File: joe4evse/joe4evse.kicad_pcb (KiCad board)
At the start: 2 copper layers, 100 x 100 mm, 85 parts, among them J1 USB_B_Micro, J10 Conn_01x02, J11 Conn_01x02, J12 Conn_02x06_Odd_Even, J13 Conn_01x03, J14 Conn_01x02, J2 Conn_01x03, J3 Conn_01x03, J4 Conn_01x02, J5 Conn_01x03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

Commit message: joe/pcb: Rev 1.1
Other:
- board text added: "Dalton EVSE "Joe" Board rev. 1.1 (c) Tuetuopay 2019-2020"
- board text removed: "Dalton EVSE "Joe" Board rev. 1.0 (c) Tuetuopay 2019"
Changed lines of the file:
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@@
     (effects (font (size 1 1) (thickness 0.15)))
   )
-  (gr_text "Dalton EVSE\n\"Joe\" Board rev. 1.0\n(c) Tuetuopay 2019" (at 182 132.4) (layer F.SilkS)
+  (gr_text "Dalton EVSE\n\"Joe\" Board rev. 1.1\n(c) Tuetuopay 2019-2020" (at 180.9 132.4) (layer F.SilkS)
     (effects (font (size 1 1) (thickness 0.15)) (justify left))
   )

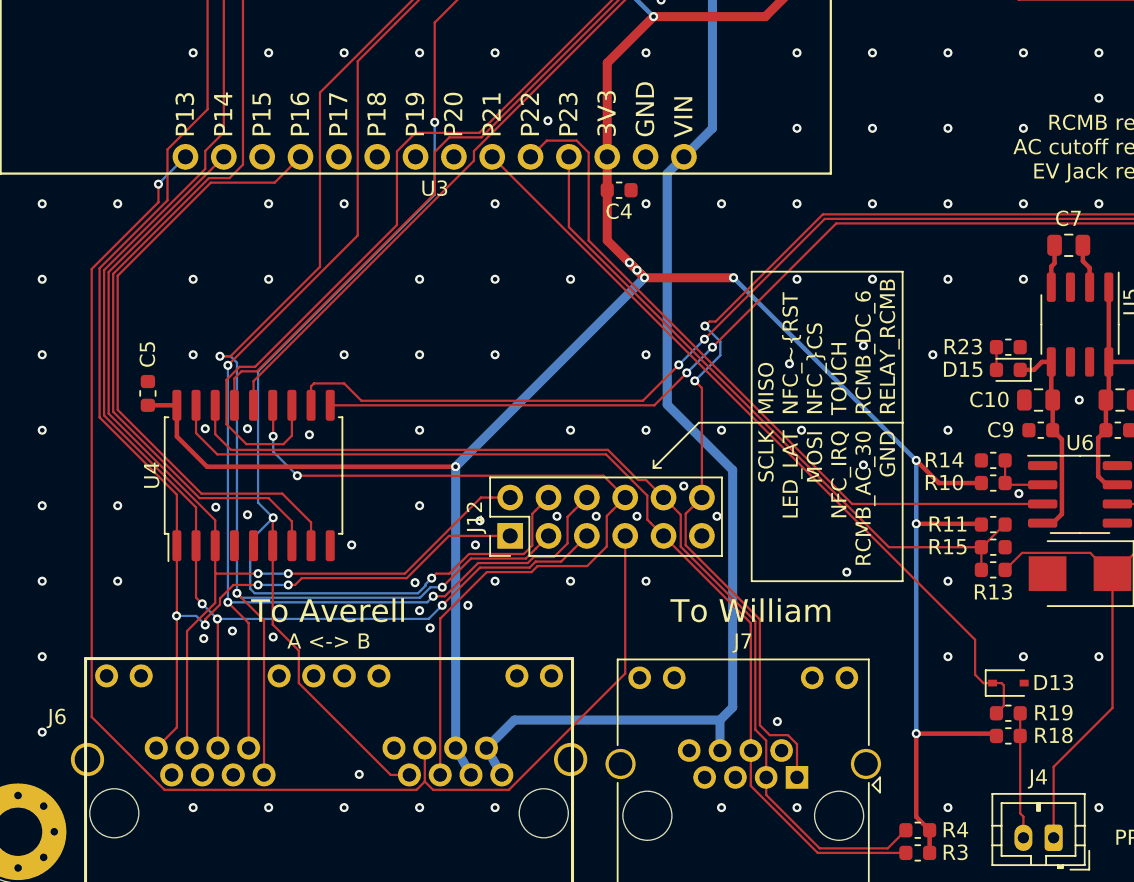
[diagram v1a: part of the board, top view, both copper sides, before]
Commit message: joe/{sch, pcb}: Swap some MCU pins for easier pinout
- Swap P23/P13
- Swap P21/P16
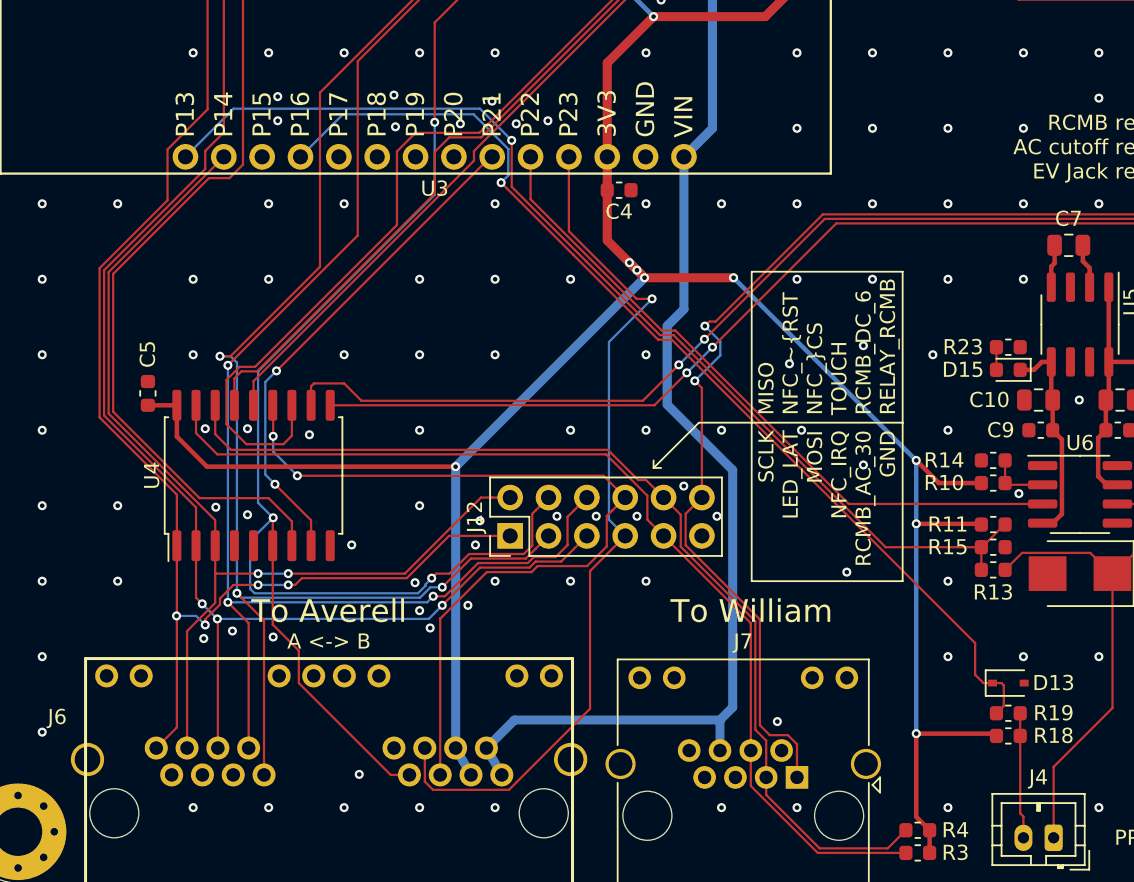
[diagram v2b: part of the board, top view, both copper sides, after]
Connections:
- U3 pad 15: /NFC_IRQ -> /fipy/PILOT_IN
- U3 pad 18: /fipy/IO_IRQ -> /fipy/PP_IN
- U3 pad 23: /fipy/PP_IN -> /fipy/IO_IRQ
- U3 pad 25: /fipy/PILOT_IN -> /NFC_IRQ
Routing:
- net /NFC_IRQ: track 92.0 -> 57.7 mm
- net /fipy/PILOT_IN: track 44.5 -> 71.6 mm, vias 0 -> 1
- net /fipy/PP_IN: track 51.8 -> 68.7 mm, vias 0 -> 1
- net /fipy/IO_IRQ: track 41.7 -> 33.3 mm, vias 0 -> 2
- net /evse/PILOT_IN: track 47.8 -> 45.1 mm
- net GND: vias 213 -> 220

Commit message: joe/pcb: Fix D13 footprint
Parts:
- D13: footprint Diode_SMD:D_SOD-323 -> Diode_SMD:D_SOD-123
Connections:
- U4 pad 8: /fipy/IO_IRQ -> Net-(U4-Pad8)

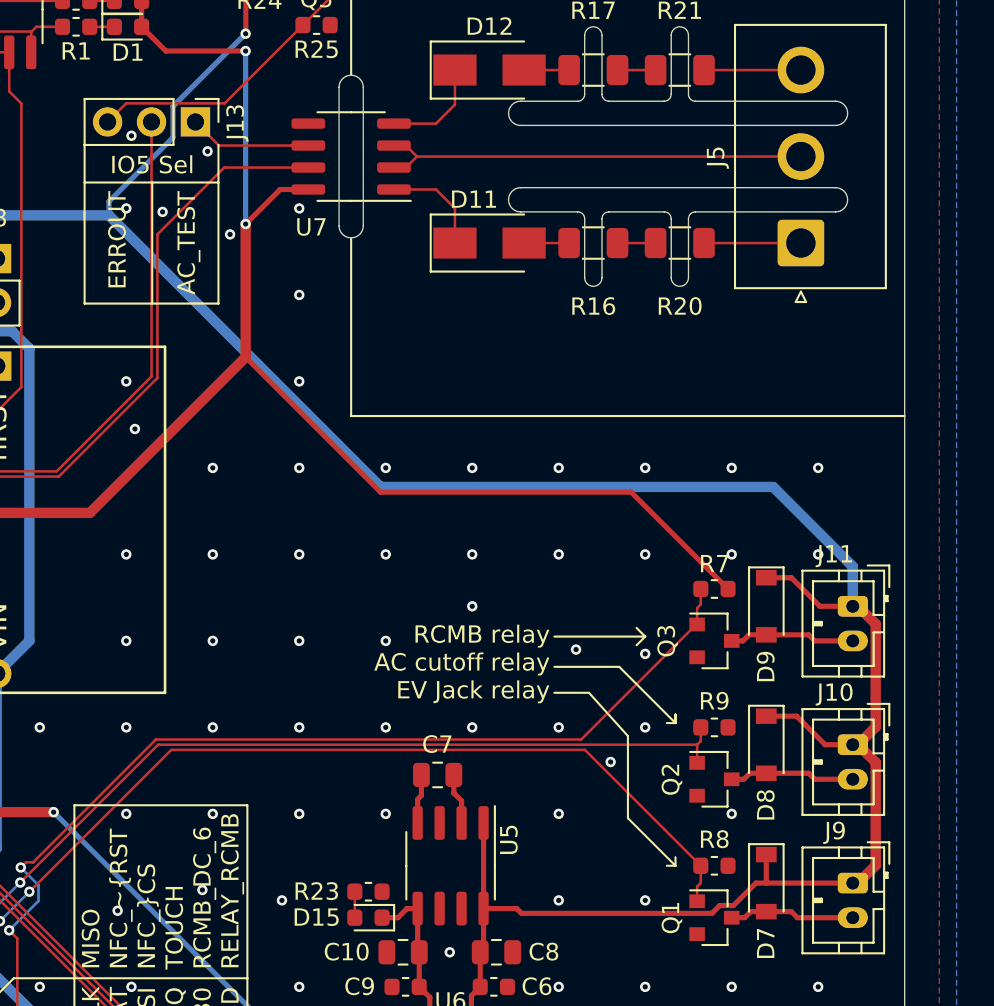
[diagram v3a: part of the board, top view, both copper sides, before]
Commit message: joe/{sch, pcb}: Combine AC_RELAY and RCMB output
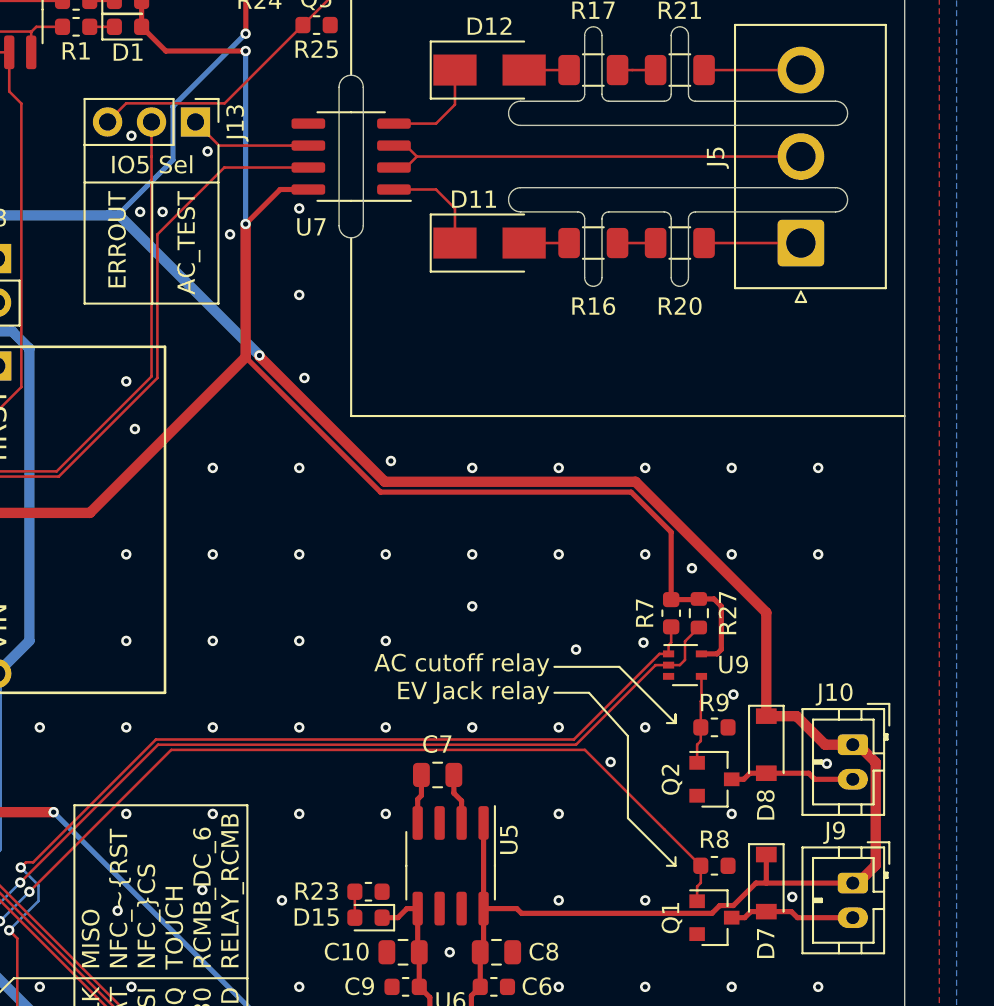
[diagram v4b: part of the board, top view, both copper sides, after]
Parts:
- removed D9: D_Schottky, Diode_SMD:D_SOD-123
- removed J11: Conn_01x02, Connector_JST:JST_PH_B2B-PH-K_1x02_P2.00mm_Vertical
- removed Q3: AO3402, Package_TO_SOT_SMD:SOT-23
- added R27: 10k, Resistor_SMD:R_0603_1608Metric, F.Cu at (188.1, 98.4)
- added U9: 74LVC1G02, Package_TO_SOT_SMD:SOT-353_SC-70-5, F.Cu at (187.3, 101.4)
- moved R7 2.87 mm to (186.5, 98.4), turned to 270 degrees
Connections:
- Q2 pad 1: /RELAY_AC -> Net-(Q2-Pad1)
- R7 pad 1: /RELAY_RCMB -> +3V3
- R7 pad 2: +3V3 -> /RELAY_RCMB
- R9 pad 2: /RELAY_AC -> Net-(Q2-Pad1)
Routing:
- net +12V: track 203.3 -> 188.5 mm, vias 4 -> 5
- net Net-(D9-Pad2): track 7.29 -> 0.00 mm
- net +3V3: track 298.5 -> 304.6 mm
- net Net-(Q2-Pad1): track 0.00 -> 5.10 mm
- net /RELAY_RCMB: track 82.5 -> 79.6 mm
- net /RELAY_AC: track 74.1 -> 75.5 mm
- net GND: vias 220 -> 224
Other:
- board text added: "AC cutoff relay EV Jack relay"
- board text removed: "RCMB relay AC cutoff relay EV Jack relay"

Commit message: joe/{sch, pcb}: Remove input shottky diodes
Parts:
- removed D3, D4: D_Schottky, Diode_SMD:D_SOD-123
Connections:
- J3 pad 2: Net-(D4-Pad2) -> +5V
- J3 pad 3: Net-(D3-Pad2) -> +12V
- U4 pad 8: Net-(U4-Pad8) -> /fipy/IO_IRQ
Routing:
- net +12V: track 188.5 -> 202.0 mm
- net +5V: track 168.3 -> 175.6 mm
- net Net-(D4-Pad2): track 4.00 -> 0.00 mm
- net Net-(D3-Pad2): track 4.00 -> 0.00 mm

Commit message: joe/pcb: Rev 1.2
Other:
- board text added: "Dalton EVSE "Joe" Board rev. 1.2 (c) Tuetuopay 2019-2021"
- board text removed: "Dalton EVSE "Joe" Board rev. 1.1 (c) Tuetuopay 2019-2020"
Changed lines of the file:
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@@
     (effects (font (size 1 1) (thickness 0.15)))
   )
-  (gr_text "Dalton EVSE\n\"Joe\" Board rev. 1.1\n(c) Tuetuopay 2019-2020" (at 180.9 132.4) (layer F.SilkS)
+  (gr_text "Dalton EVSE\n\"Joe\" Board rev. 1.2\n(c) Tuetuopay 2019-2021" (at 180.9 132.4) (layer F.SilkS)
     (effects (font (size 1 1) (thickness 0.15)) (justify left))
   )

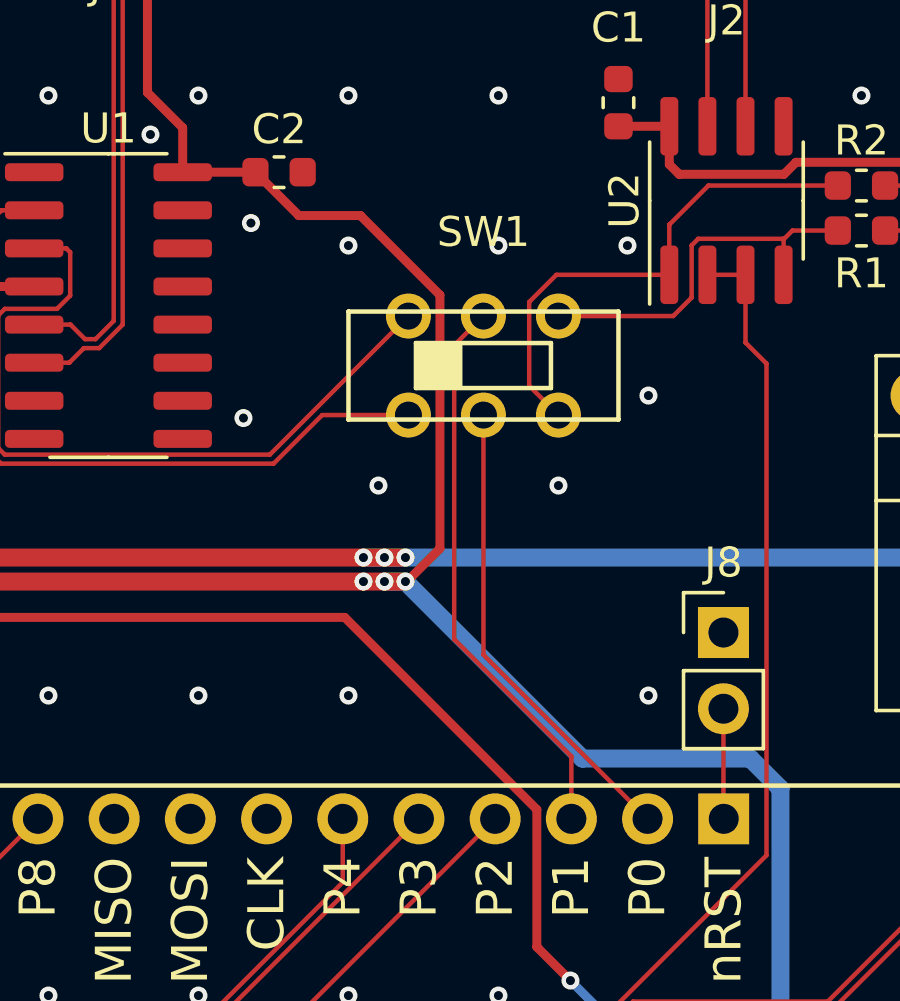
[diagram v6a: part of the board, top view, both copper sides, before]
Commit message: joe/{sch, pcb}: Add 0r resistors in parallel of SW1 for prod boards
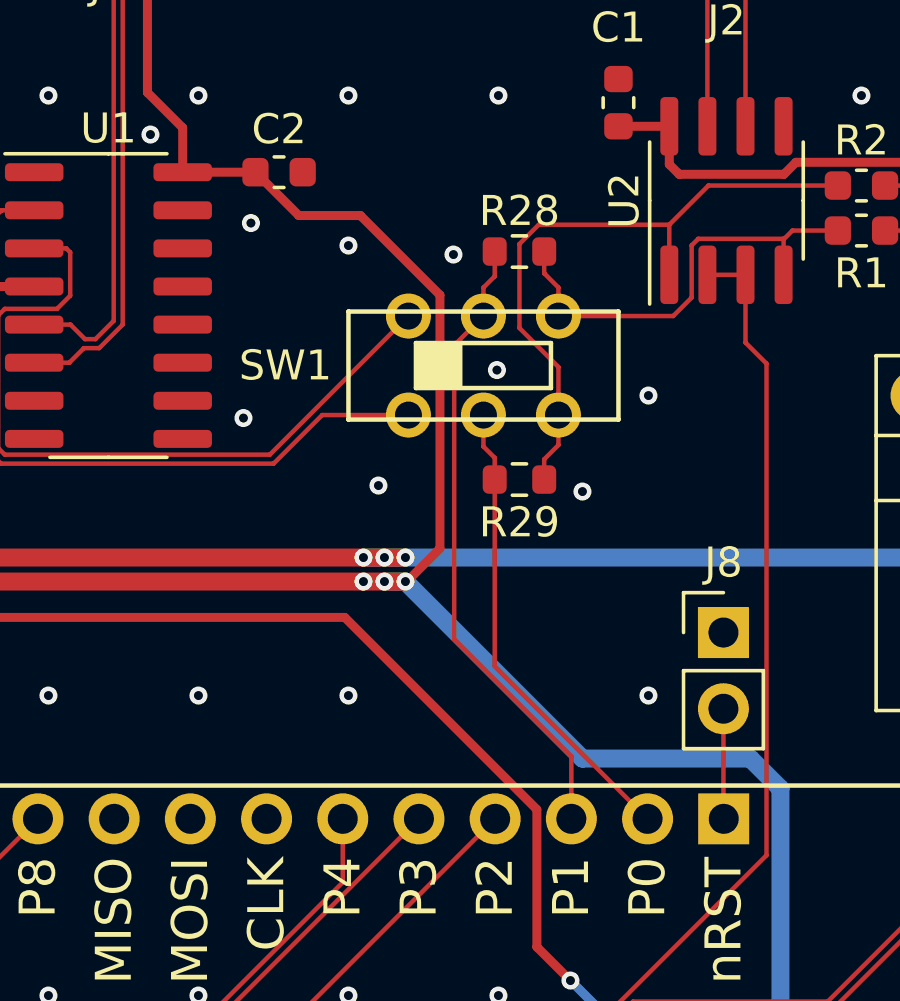
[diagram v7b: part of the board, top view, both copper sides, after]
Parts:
- added R28: 0, Resistor_SMD:R_0603_1608Metric, F.Cu at (140.7, 65.2)
- added R29: 0, Resistor_SMD:R_0603_1608Metric, F.Cu at (140.7, 72.8)
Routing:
- net /MOD_TX: track 17.0 -> 21.7 mm
- net /MOD_RX: track 12.7 -> 15.1 mm
- net /FIPY_TXD: track 18.8 -> 21.1 mm

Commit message: joe/pcb: Rev v1.3
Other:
- board text added: "Dalton EVSE "Joe" Board rev. 1.3 (c) Tuetuopay 2019-2021"
- board text removed: "Dalton EVSE "Joe" Board rev. 1.2 (c) Tuetuopay 2019-2021"
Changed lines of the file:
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@@
     (effects (font (size 1 1) (thickness 0.15)))
   )
-  (gr_text "Dalton EVSE\n\"Joe\" Board rev. 1.2\n(c) Tuetuopay 2019-2021" (at 180.9 132.4) (layer F.SilkS)
+  (gr_text "Dalton EVSE\n\"Joe\" Board rev. 1.3\n(c) Tuetuopay 2019-2021" (at 180.9 132.4) (layer F.SilkS)
     (effects (font (size 1 1) (thickness 0.15)) (justify left))
   )
